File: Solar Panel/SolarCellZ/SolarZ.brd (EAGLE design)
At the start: 91.1 x 91 mm, 34 parts, among them X1 BU-SMA-V

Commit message: Routing on draft Z panel - dimensions need to be confirmed
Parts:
- removed F1: (no value), pandasat:BURN_WIRE
- removed J1: (no value), pandasat:2X3
- added F2: (no value), pandasat:BURN_WIRE
- added U$4: M20-8760342, Solar:M20-8760342
- moved D6 172.7 mm to (81.1, 14.3), turned to 270 degrees
- moved D7 166.3 mm to (21.4, 73.6), turned to 180 degrees
- moved D5 163.4 mm to (73.0, 71.2), turned to 270 degrees
- moved D10 149.5 mm to (11.1, 11.2), turned to 180 degrees
- moved D9 134.9 mm to (18.4, 10.0), turned to 90 degrees
- moved D1 122.5 mm to (84.2, 53.4), turned to 270 degrees
- moved D8 111.2 mm to (24.2, 6.60), turned to 180 degrees
- moved D3 97.1 mm to (52.2, 74.5), turned to 90 degrees
- moved D2 93.8 mm to (41.3, 56.0), turned to 90 degrees
- moved 10 90.7 mm to (5.60, 65.2)
- moved 4 86.3 mm to (50.5, 77.5)
- moved 14 74.4 mm to (8.80, -4.60), turned to 0 degrees
- moved 9 74.0 mm to (63.7, -4.20), turned to 40 degrees
- moved 5 71.8 mm to (26.9, 72.1)
- moved 11 69.2 mm to (14.9, 63.9), turned to 0 degrees
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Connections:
- removed net N$1 (its old number): J1.2, J1.3
- removed net N$13: 17.P$1, 18.P$1, D10.POS
- removed net N$4: U$1.2, U$2.RF, U$2.RF_2
- removed net N$5: U$1.1, U$3.RF, U$3.RF_2
- removed net VBURN: F1.1, F1.10, F1.100, J1.4, J1.6
- new net N$16: F2.1, F2.10, F2.100, U$4.P$4, U$4.P$6
- new net N$8: U$4.P$2, U$4.P$3
- new net N$9: 10.P$1, 11.P$1, 6.P$2, 7.P$2, D4.NEG, D7.POS
- new net RF_P: U$1.2, U$3.RF, U$3.RF_2
- net GND: now also 17.P$1, 18.P$1, D10.POS, F2.2, F2.20, F2.200, U$4.P$1; no longer 6.P$1, 7.P$1, D4.POS, F1.2, F1.20, F1.200, J1.1
- net N$11: now also 6.P$1, 7.P$1, D4.POS; no longer 10.P$1, 11.P$1, D7.POS
- net N$3: now also U$1.1, U$2.RF, U$2.RF_2; no longer 6.P$2, 7.P$2, D4.NEG
- net VSOLAR: now also U$4.P$5; no longer J1.5
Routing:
- net N$11: track 0.00 -> 148.0 mm
- net N$9: track 0.00 -> 122.9 mm
- net N$18: track 0.00 -> 91.2 mm
- net N$12: track 0.00 -> 63.1 mm
- net N$6: track 0.00 -> 62.4 mm
- net N$10: track 0.00 -> 56.8 mm
- net N$16: track 0.00 -> 50.3 mm, vias 0 -> 1
- net N$14: track 0.00 -> 49.9 mm
- net N$1: track 0.00 -> 45.6 mm
- net GND: track 0.00 -> 43.9 mm
- net N$7: track 0.00 -> 23.5 mm
- net RF_P: track 0.00 -> 17.7 mm
- net N$3: track 0.00 -> 17.3 mm
- net VSOLAR: track 0.00 -> 7.27 mm
- net N$2: track 0.00 -> 5.29 mm

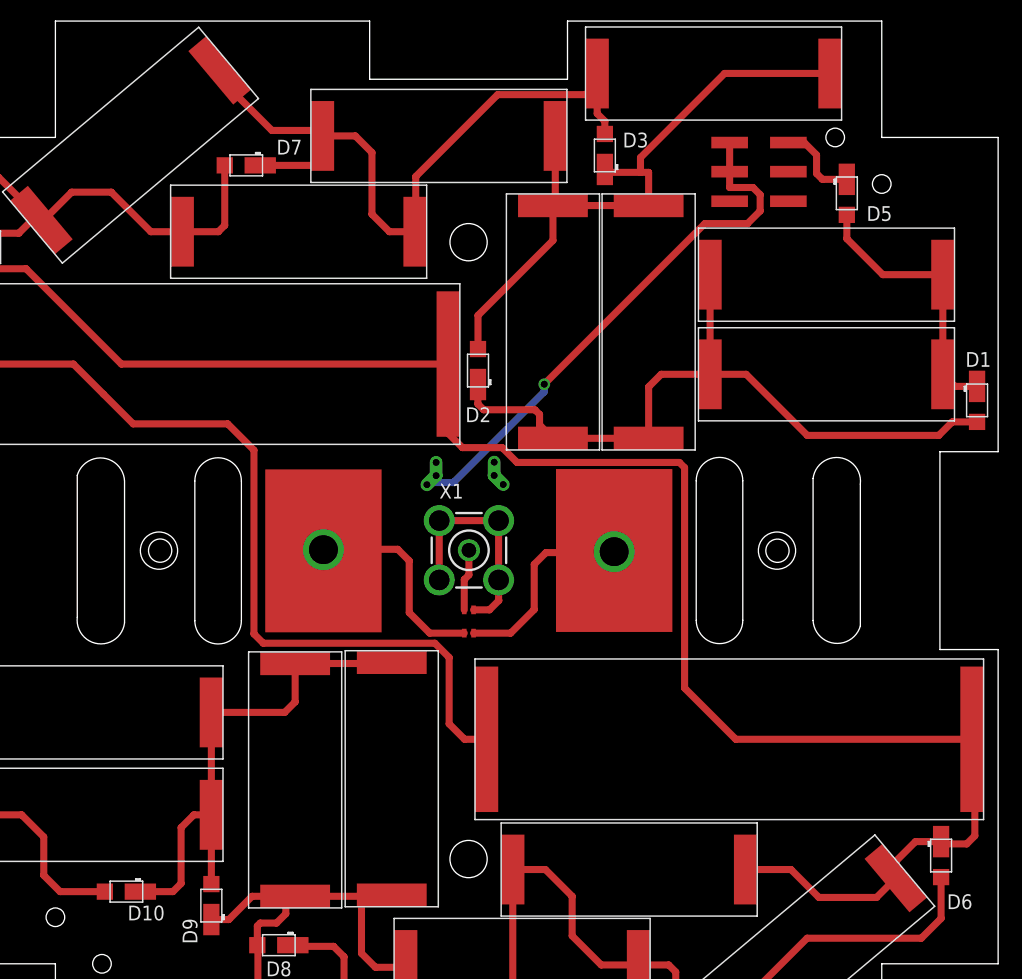
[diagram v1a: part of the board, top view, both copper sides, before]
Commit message: Some Magnetorquer routing
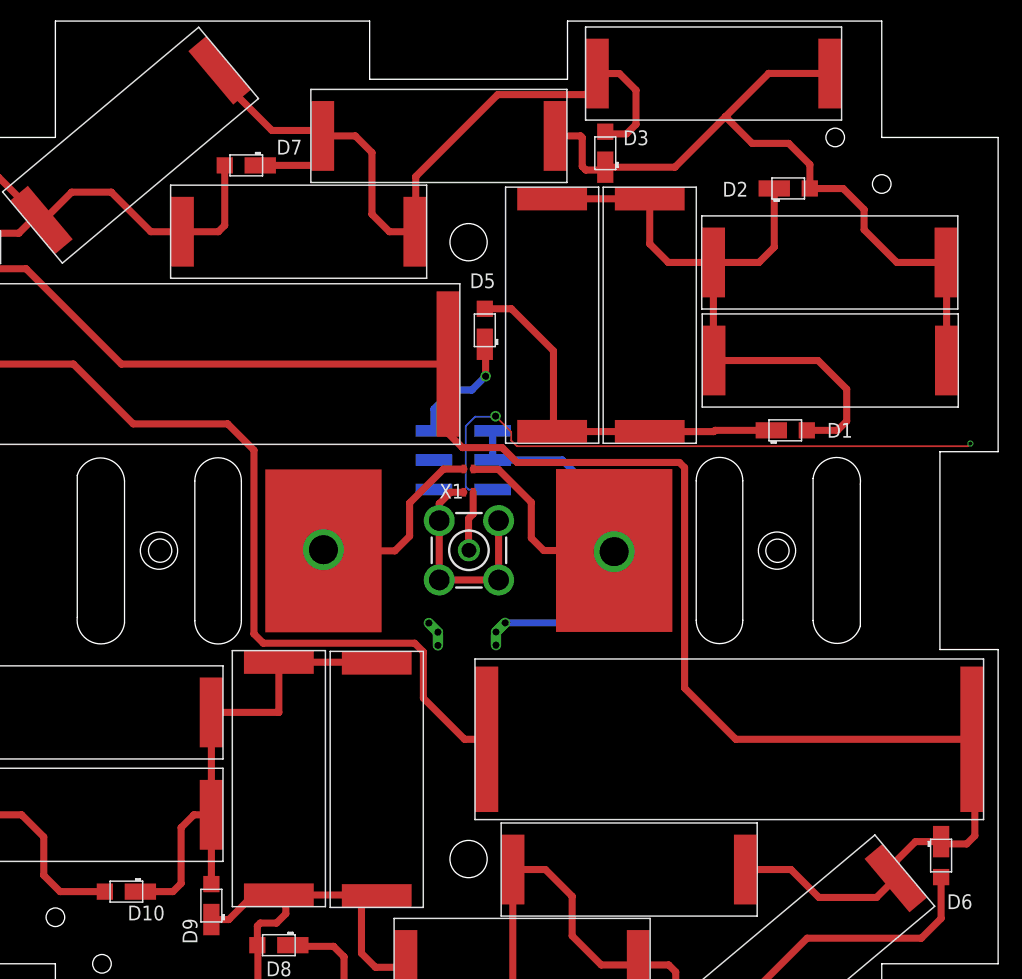
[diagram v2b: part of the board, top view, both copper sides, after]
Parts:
- moved U$4 41.8 mm to (35.9, 45.2), flipped to the bottom
- moved 13 40.2 mm to (82.6, 60.8), turned to 180 degrees
- moved D5 33.3 mm to (41.9, 59.4), turned to 90 degrees
- moved D2 30.9 mm to (68.0, 71.6), turned to 0 degrees
- moved 1 30.6 mm to (82.5, 69.3), turned to 180 degrees
- moved 3 21.7 mm to (52.1, 71.7), turned to 270 degrees
- moved 2 20.2 mm to (43.7, 71.7), turned to 270 degrees
- moved D1 16.7 mm to (67.7, 50.8), turned to 0 degrees
- moved F2 16.5 mm to (37.9, 32.4), turned to 180 degrees
- moved U$1 12.1 mm to (40.5, 46.5), turned to 0 degrees
- moved 15 1.40 mm to (20.2, 31.9)
- moved 16 1.29 mm to (28.6, 31.8)
- moved D3 0.20 mm to (52.2, 74.6)
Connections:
- removed net RF_P: U$1.2, U$3.RF, U$3.RF_2
- new net N$4: U$1.1, U$3.RF, U$3.RF_2
- net N$3: now also U$1.2; no longer U$1.1
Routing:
- net N$8: track 0.00 -> 7354.4 mm, vias 0 -> 2
- net N$16: track 50.3 -> 32.2 mm, vias 1 -> 0
- net RF_P: track 17.7 -> 0.00 mm
- net N$4: track 0.00 -> 16.7 mm
- net N$7: track 23.5 -> 33.3 mm
- net N$10: track 56.8 -> 64.5 mm
- net N$6: track 62.4 -> 56.6 mm
- net N$12: track 63.1 -> 68.1 mm
- net VSOLAR: track 7.27 -> 10.3 mm, vias 0 -> 1
- net GND: track 43.9 -> 45.8 mm
- net N$14: track 49.9 -> 50.9 mm
- net N$9: track 122.9 -> 121.9 mm
- net N$1: track 45.6 -> 44.9 mm

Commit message: Magnetorquers done
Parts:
- removed 15, 16, 17, 18: KXOB22-04X3F, Solar:KXOB22-04X3F
- removed D10, D9: SB_DIODE, Solar:SB_DIODE
- added F1: (no value), pandasat:BURN_WIRE
- 12, 14, 2, 3, 4, 5, 8, 9: value KXOB22-04X3F -> SLMD121H04L; device Solar:KXOB22-04X3F -> Solar:SLMD121H04L
- 6, 7: value SLMD121H04L -> KXOB22-04X3F; device Solar:SLMD121H04L -> Solar:KXOB22-04X3F
- moved D4 84.1 mm to (57.3, 5.61), turned to 180 degrees
- moved 6 72.3 mm to (85.5, 7.36)
- moved D7 68.7 mm to (34.4, 6.10)
- moved 7 62.3 mm to (27.2, 7.36)
- moved 1 59.8 mm to (27.0, 91.2)
- moved 3 55.9 mm to (-3.73, 68.5), turned to 0 degrees
- moved F2 52.4 mm to (42.9, 84.5)
- moved 2 50.6 mm to (-3.69, 54.1), turned to 0 degrees
- moved 10 50.0 mm to (41.2, 30.1), turned to 270 degrees
- moved D1 47.7 mm to (33.8, 84.4), turned to 180 degrees
- moved 12 43.6 mm to (-3.75, 22.5)
- moved D6 38.1 mm to (48.4, 33.8)
- moved 11 34.4 mm to (49.2, 60.5), turned to 90 degrees
- moved D8 32.7 mm to (42.0, 34.0), turned to 90 degrees
- moved 13 30.4 mm to (85.6, 91.1)
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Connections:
- removed net N$14: 12.P$1, 14.P$1, 15.P$2, 16.P$2, D8.POS, D9.NEG
- removed net N$18: 12.P$2, 14.P$2, 8.P$1, 9.P$1, D6.POS, D8.NEG
- removed net N$4: U$1.1, U$3.RF, U$3.RF_2
- new net N8: 12.P$1, 14.P$1, 6.P$2, 7.P$2, D4.NEG, D8.POS
- net GND: now also 8.P$1, 9.P$1, D6.POS, F1.2, F1.20, F1.200; no longer 17.P$1, 18.P$1, D10.POS
- net N$1: now also U$1.2, U$3.RF, U$3.RF_2; no longer 15.P$1, 16.P$1, 17.P$2, 18.P$2, D10.NEG, D9.POS
- net N$16: now also F1.1, F1.10, F1.100
- net N$3: now also U$1.1; no longer U$1.2
- net N$9: now also 12.P$2, 14.P$2, D8.NEG; no longer 6.P$2, 7.P$2, D4.NEG
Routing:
- net N$8: track 7354.4 -> 44659.3 mm, vias 2 -> 4
- net N8: track 0.00 -> 152.2 mm
- net N$10: track 64.5 -> 161.6 mm
- net N$18: track 91.2 -> 0.00 mm
- net N$16: track 32.2 -> 118.5 mm, vias 0 -> 2
- net N$6: track 56.6 -> 109.8 mm
- net N$12: track 68.1 -> 121.0 mm, vias 0 -> 2
- net N$14: track 50.9 -> 0.00 mm
- net N$9: track 121.9 -> 80.3 mm, vias 0 -> 2
- net N$1: track 44.9 -> 19.4 mm
- net N$4: track 16.7 -> 0.00 mm
- net GND: track 45.8 -> 39.3 mm, vias 0 -> 2
- net VSOLAR: track 10.3 -> 7.40 mm
- net N$3: track 16.8 -> 19.4 mm
- net N$7: track 33.3 -> 31.2 mm
- added copper zone on layer 1, net GND
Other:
- board size 91.1 x 91 mm -> 99 x 99 mm

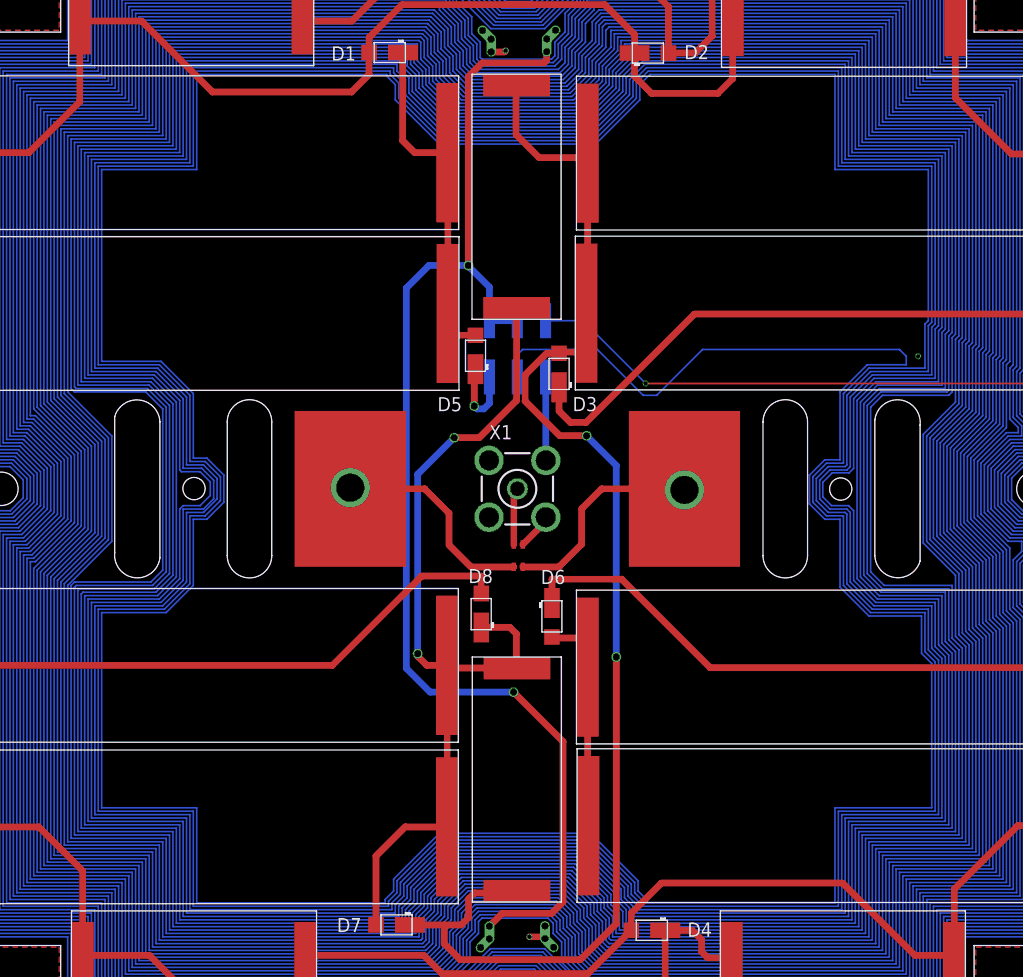
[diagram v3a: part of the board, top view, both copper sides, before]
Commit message: Added space around cutouts
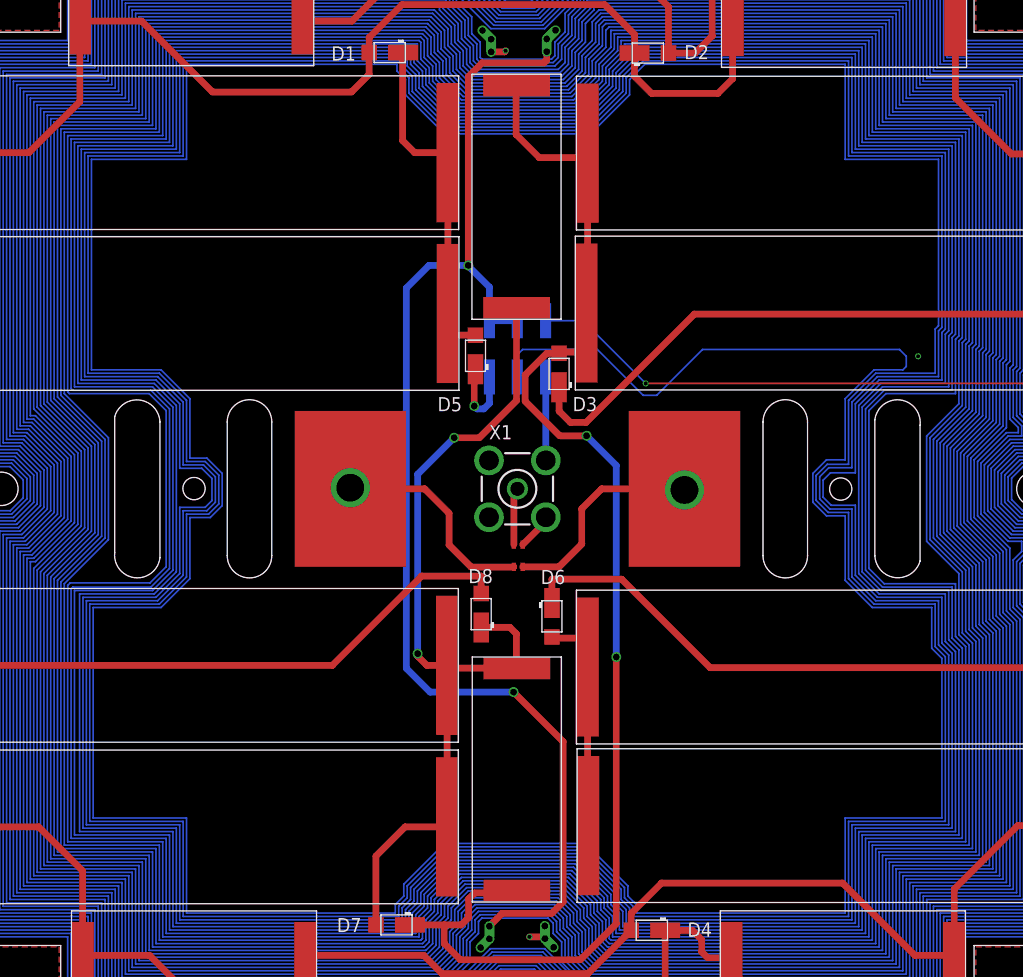
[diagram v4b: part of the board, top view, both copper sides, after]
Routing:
- net N$8: track 44659.3 -> 41368.0 mm

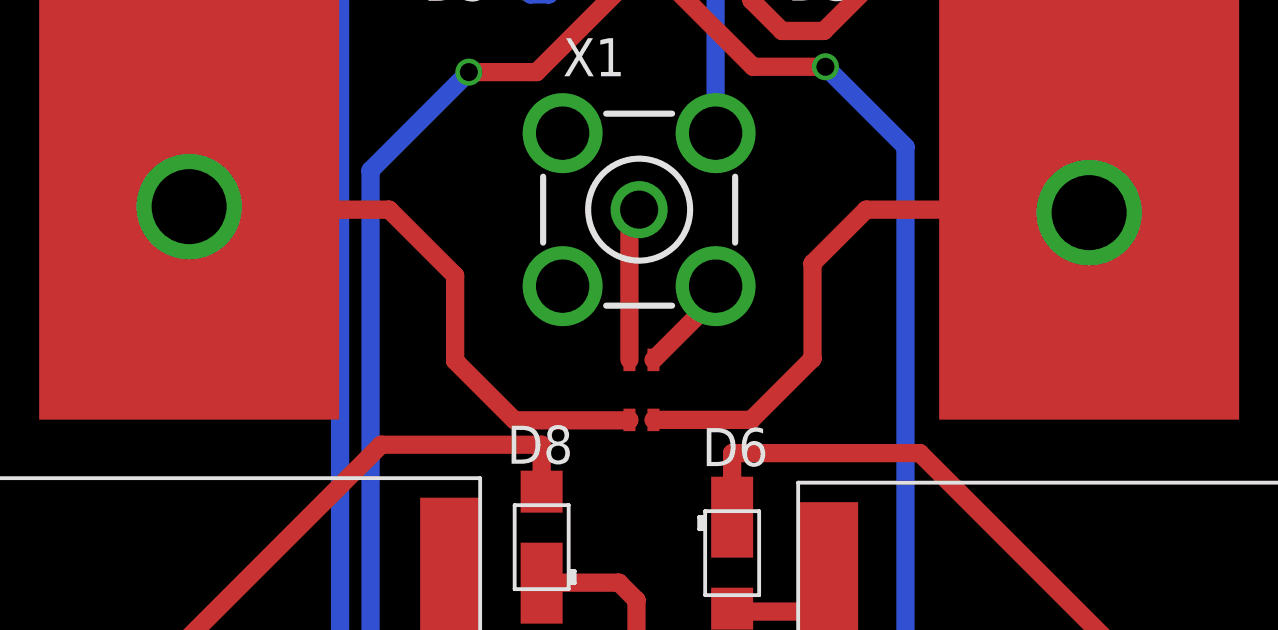
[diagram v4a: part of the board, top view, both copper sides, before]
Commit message: Changed RF trace width
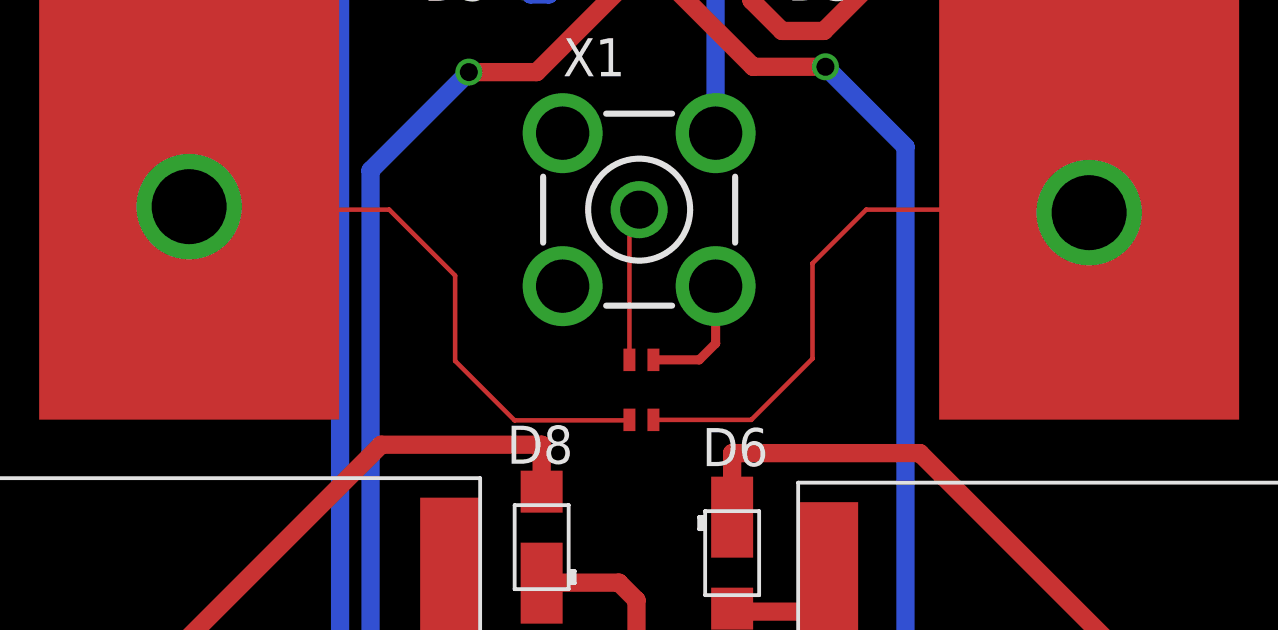
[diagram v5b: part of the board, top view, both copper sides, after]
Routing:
- net GND: track 39.3 -> 40.2 mm
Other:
- board text added: "PandaSat Solar Panel Z"
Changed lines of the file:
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@@
 <grid distance="6" unitdist="mil" unit="mil" style="lines" multiple="1" display="yes" altdistance="5" altunitdist="mil" altunit="mil"/>
 <layers>
-<layer number="1" name="Top" color="4" fill="1" visible="no" active="yes"/>
+<layer number="1" name="Top" color="4" fill="1" visible="yes" active="yes"/>
 <layer number="2" name="Route2" color="16" fill="1" visible="yes" active="yes"/>
 <layer number="3" name="Route3" color="17" fill="1" visible="no" active="no"/>
@@
 <circle x="91.575" y="45.25" radius="2.75" width="0.001" layer="39"/>
 <circle x="91.575" y="45.25" radius="2.75" width="0.001" layer="40"/>
+<text x="32.3088" y="14.9352" size="1.778" layer="22" rot="MR0">PandaSat
+Solar Panel Z</text>
 </plain>
 <attributes>
@@
 <wire x1="51.55" y1="29.25" x2="51.55" y2="15.071" width="0.6096" layer="1"/>
 <wire x1="51.55" y1="15.071" x2="51.6085" y2="15.0125" width="0.6096" layer="1"/>
-<wire x1="45.7269" y1="40.2429" x2="47.7999" y2="42.3159" width="0.6096" layer="1"/>
-<wire x1="47.7999" y1="42.3159" x2="47.7999" y2="42.7001" width="0.6096" layer="1"/>
+<wire x1="45.7269" y1="40.2429" x2="47.2533" y2="40.2429" width="0.3048" layer="1"/>
+<wire x1="47.2533" y1="40.2429" x2="47.7999" y2="40.7895" width="0.3048" layer="1"/>
+<wire x1="47.7999" y1="40.7895" x2="47.7999" y2="40.789465625" width="0.3048" layer="1"/>
+<wire x1="47.7999" y1="40.789465625" x2="47.7999" y2="42.7001" width="0.3048" layer="1"/>
 <polygon width="0.001" layer="1">
 <vertex x="4.1148" y="94.9452"/>
@@
 <contactref element="X1" pad="1"/>
 <contactref element="U$1" pad="4"/>
-<wire x1="44.9269" y1="40.2429" x2="44.9269" y2="44.9269" width="0.6096" layer="1"/>
-<wire x1="44.9269" y1="44.9269" x2="45.25" y2="45.25" width="0.6096" layer="1"/>
+<wire x1="44.9269" y1="40.2429" x2="44.9269" y2="44.9269" width="0.1524" layer="1"/>
+<wire x1="44.9269" y1="44.9269" x2="45.25" y2="45.25" width="0.1524" layer="1"/>
 </signal>
 <signal name="N$10">
@@
 <contactref element="U$3" pad="RF_2"/>
 <contactref element="U$1" pad="2"/>
-<wire x1="44.911" y1="38.227" x2="44.9269" y2="38.2429" width="0.6096" layer="1"/>
-<wire x1="41.0972" y1="38.227" x2="44.911" y2="38.227" width="0.6096" layer="1"/>
-<wire x1="30.25" y1="45.25" x2="36.919" y2="45.25" width="0.6096" layer="1"/>
-<wire x1="39.116" y1="43.053" x2="39.116" y2="40.2082" width="0.6096" layer="1"/>
-<wire x1="39.116" y1="40.2082" x2="41.0972" y2="38.227" width="0.6096" layer="1"/>
-<wire x1="36.919" y1="45.25" x2="39.116" y2="43.053" width="0.6096" layer="1"/>
+<wire x1="44.911" y1="38.227" x2="44.9269" y2="38.2429" width="0.1524" layer="1"/>
+<wire x1="41.0972" y1="38.227" x2="44.911" y2="38.227" width="0.1524" layer="1"/>
+<wire x1="30.25" y1="45.25" x2="36.919" y2="45.25" width="0.1524" layer="1"/>
+<wire x1="39.116" y1="43.053" x2="39.116" y2="40.2082" width="0.1524" layer="1"/>
+<wire x1="39.116" y1="40.2082" x2="41.0972" y2="38.227" width="0.1524" layer="1"/>
+<wire x1="36.919" y1="45.25" x2="39.116" y2="43.053" width="0.1524" layer="1"/>
 <wire x1="30.25" y1="45.25" x2="30.25" y2="45.35" width="0.6096" layer="1"/>
 </signal>
@@
 <contactref element="U$2" pad="RF_2"/>
 <contactref element="U$1" pad="1"/>
-<wire x1="60.25" y1="45.25" x2="52.8192" y2="45.25" width="0.6096" layer="1"/>
-<wire x1="51.0286" y1="43.4594" x2="51.0286" y2="40.2844" width="0.6096" layer="1"/>
-<wire x1="48.9871" y1="38.2429" x2="45.7269" y2="38.2429" width="0.6096" layer="1"/>
-<wire x1="51.0286" y1="40.2844" x2="48.9871" y2="38.2429" width="0.6096" layer="1"/>
-<wire x1="52.8192" y1="45.25" x2="51.0286" y2="43.4594" width="0.6096" layer="1"/>
+<wire x1="60.25" y1="45.25" x2="52.8192" y2="45.25" width="0.1524" layer="1"/>
+<wire x1="51.0286" y1="43.4594" x2="51.0286" y2="40.2844" width="0.1524" layer="1"/>
+<wire x1="48.9871" y1="38.2429" x2="45.7269" y2="38.2429" width="0.1524" layer="1"/>
+<wire x1="51.0286" y1="40.2844" x2="48.9871" y2="38.2429" width="0.1524" layer="1"/>
+<wire x1="52.8192" y1="45.25" x2="51.0286" y2="43.4594" width="0.1524" layer="1"/>
 <wire x1="60.25" y1="45.25" x2="60.25" y2="45.15" width="0.6096" layer="1"/>
 </signal>
@@
 </board>
 </drawing>
+<compatibility>
+<note version="6.3" minversion="6.2.2" severity="warning">
+Since Version 6.2.2 text objects can contain more than one line,
+which will not be processed correctly with this version.
+</note>
+</compatibility>
 </eagle>

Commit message: Changed Z panel hole
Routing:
- net N$8: track 41368.0 -> 41447.2 mm
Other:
- board text added: "PandaSat Solar Panel Z Rev A"
- board text removed: "PandaSat Solar Panel Z"
